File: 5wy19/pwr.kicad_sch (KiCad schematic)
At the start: 1 part, among them IC7 A2C20219

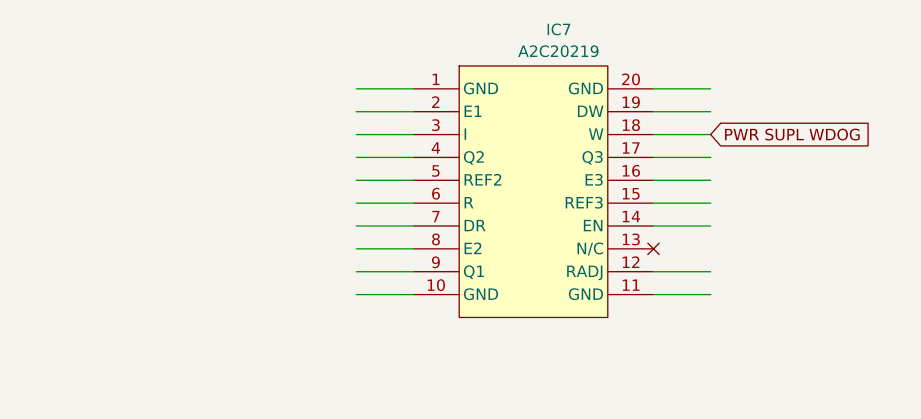
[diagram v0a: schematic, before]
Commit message: Mapped out more pins of MCU and relevant circuits
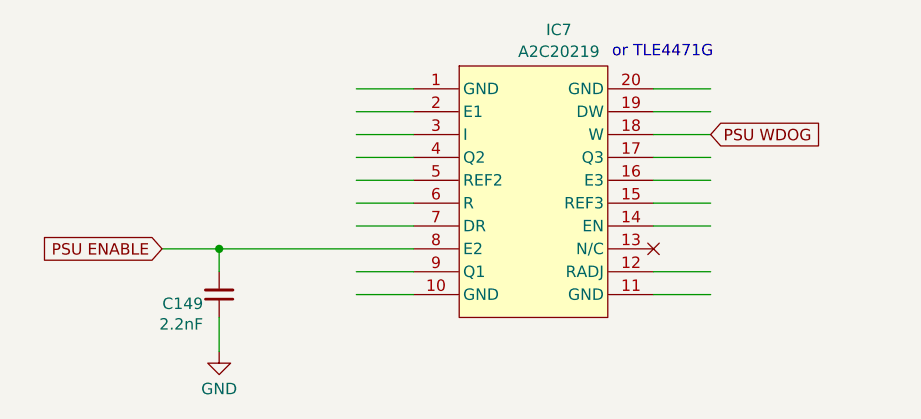
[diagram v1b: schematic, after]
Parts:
- added C149: 2.2nF, symbol Device:C_Small
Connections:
- net PSU ENABLE: now reaches IC7.8 (E2)
- net PSU ENABLE: now also C149.2
- net PWR SUPL WDOG renamed PSU WDOG
- new net GND: C149.1
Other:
- note added: "or TLE4471G"
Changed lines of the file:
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@@
 	(generator_version "9.0")
 	(paper "A4")
+	(text "or TLE4471G"
+		(exclude_from_sim no)
+		(at 155.956 77.216 0)
+		(effects
+			(font
+				(size 1.27 1.27)
+			)
+		)
+	)
+	(junction
+		(at 106.68 99.06)
+		(diameter 0)
+		(color 0 0 0 0)
+	)
 	(wire
 		(pts
@@
 	(wire
 		(pts
+			(xy 106.68 106.68) (xy 106.68 110.49)
+		)
+		(stroke
+			(width 0)
+			(type default)
+		)
+	)
+	(wire
+		(pts
 			(xy 121.92 81.28) (xy 128.27 81.28)
 		)
@@
 	(wire
 		(pts
-			(xy 121.92 99.06) (xy 128.27 99.06)
+			(xy 100.33 99.06) (xy 106.68 99.06)
+		)
+		(stroke
+			(width 0)
+			(type default)
+		)
+	)
+	(wire
+		(pts
+			(xy 106.68 99.06) (xy 128.27 99.06)
+		)
+		(stroke
+			(width 0)
+			(type default)
+		)
+	)
+	(wire
+		(pts
+			(xy 106.68 99.06) (xy 106.68 101.6)
 		)
 		(stroke
@@
 		)
 	)
-	(global_label "PWR SUPL WDOG"
+	(global_label "PSU ENABLE"
+		(shape input)
+		(at 100.33 99.06 180)
+		(fields_autoplaced yes)
+		(effects
+			(font
+				(size 1.27 1.27)
+			)
+			(justify right)
+		)
+		(property "Intersheetrefs" "${INTERSHEET_REFS}"
+			(at 85.552 99.06 0)
+			(effects
+				(font
+					(size 1.27 1.27)
+				)
+				(justify right)
+				(hide yes)
+			)
+		)
+	)
+	(global_label "PSU WDOG"
 		(shape input)
 		(at 161.29 86.36 0)
@@
 				(justify left)
 				(hide yes)
+			)
+		)
+	)
+	(symbol
+		(lib_id "power:GND")
+		(at 106.68 110.49 0)
+		(unit 1)
+		(exclude_from_sim no)
+		(in_bom yes)
+		(on_board yes)
+		(dnp no)
+		(fields_autoplaced yes)
+		(property "Reference" "#PWR044"
+			(at 106.68 116.84 0)
+			(effects
+				(font
+					(size 1.27 1.27)
+				)
+				(hide yes)
+			)
+		)
+		(property "Value" "GND"
+			(at 106.68 114.6231 0)
+			(effects
+				(font
+					(size 1.27 1.27)
+				)
+			)
+		)
+		(property "Footprint" ""
+			(at 106.68 110.49 0)
+			(effects
+				(font
+					(size 1.27 1.27)
+				)
+				(hide yes)
+			)
+		)
+		(property "Datasheet" ""
+			(at 106.68 110.49 0)
+			(effects
+				(font
+					(size 1.27 1.27)
+				)
+				(hide yes)
+			)
+		)
+		(property "Description" "Power symbol creates a global label with name \"GND\" , ground"
+			(at 106.68 110.49 0)
+			(effects
+				(font
+					(size 1.27 1.27)
+				)
+				(hide yes)
+			)
+		)
+		(pin "1"
+		)
+		(instances
+			(project "5wy19_converted"
+				(path "/abd366a8-4ac6-4ee7-9079-ac453affd4f2/c4e8148c-e0d9-424a-a1b0-b7edb94ab807"
+					(reference "#PWR044")
+					(unit 1)
+				)
 			)
 		)
@@
 					(unit 1)
 				)
+			)
+		)
+	)
+	(symbol
+		(lib_id "Device:C_Small")
+		(at 106.68 104.14 180)
+		(unit 1)
+		(exclude_from_sim no)
+		(in_bom yes)
+		(on_board yes)
+		(dnp no)
+		(property "Reference" "C149"
+			(at 104.902 105.156 0)
+			(effects
+				(font
+					(size 1.27 1.27)
+				)
+				(justify left)
+			)
+		)
+		(property "Value" "2.2nF"
+			(at 104.902 107.442 0)
+			(effects
+				(font
+					(size 1.27 1.27)
+				)
+				(justify left)
+			)
+		)
+		(property "Footprint" ""
+			(at 106.68 104.14 0)
+			(effects
+				(font
+					(size 1.27 1.27)
+				)
+				(hide yes)
+			)
+		)
+		(property "Datasheet" "~"
+			(at 106.68 104.14 0)
+			(effects
+				(font
+					(size 1.27 1.27)
+				)
+				(hide yes)
+			)
+		)
+		(property "Description" "Unpolarized capacitor, small symbol"
+			(at 106.68 104.14 0)
+			(effects
+				(font
+					(size 1.27 1.27)
+				)
+				(hide yes)
+			)
+		)
+		(pin "1"
+		)
+		(pin "2"
+		)
+		(instances
+			(project "5wy19_converted"
+				(path "/abd366a8-4ac6-4ee7-9079-ac453affd4f2/c4e8148c-e0d9-424a-a1b0-b7edb94ab807"
+					(reference "C149")
+					(unit 1)
+				)

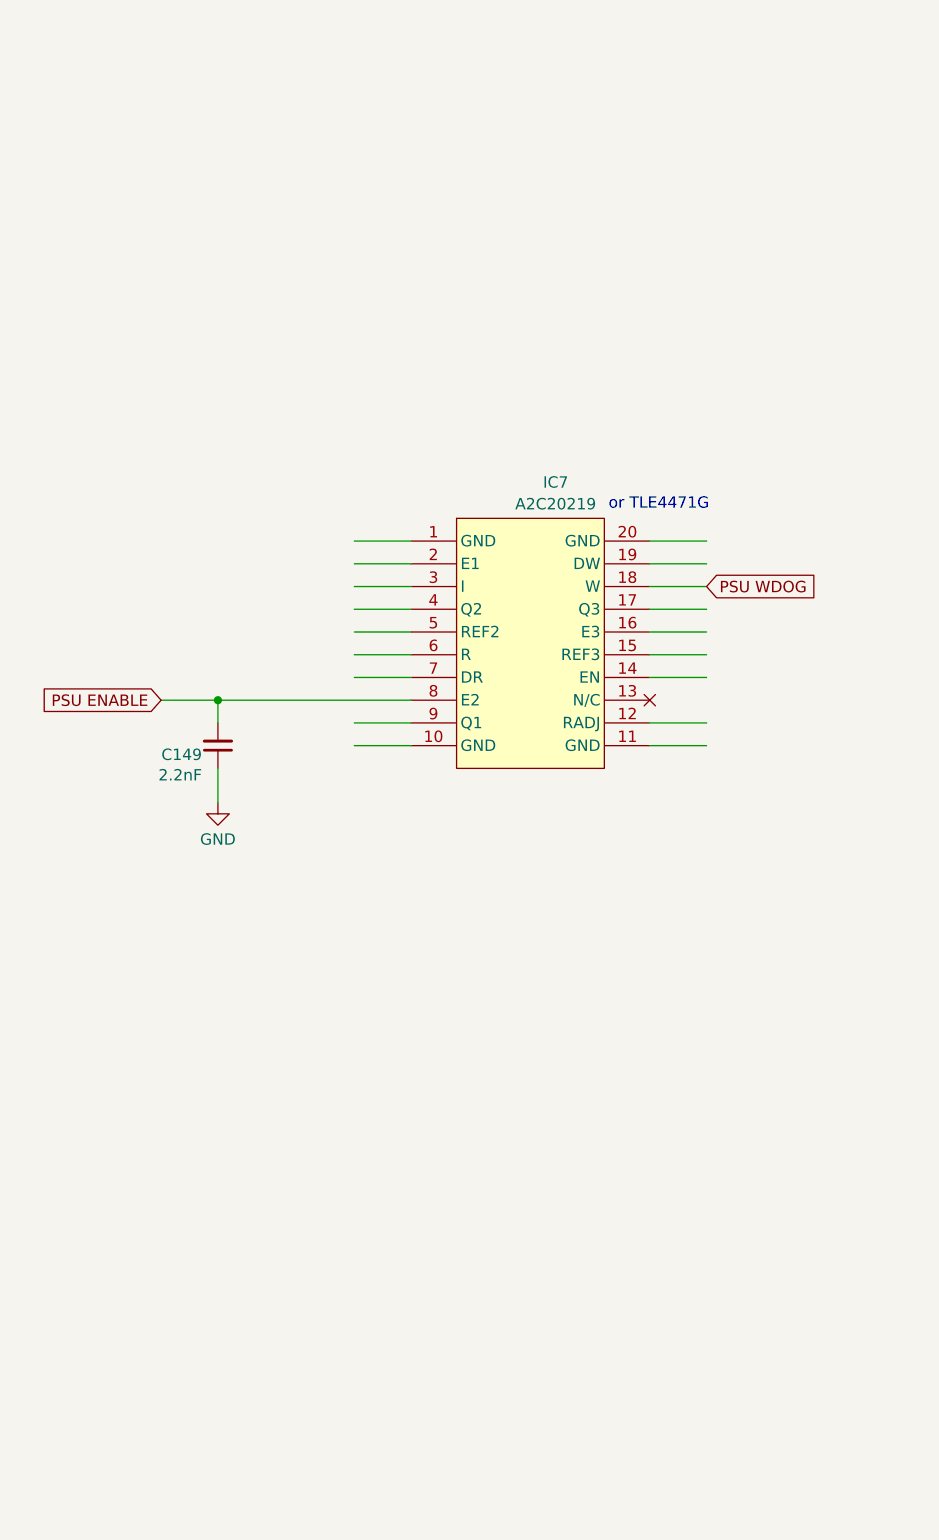
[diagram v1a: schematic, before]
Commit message: Finished most of the subsystems
-- MCU finished
-- Flash finished
-- Power Supply finished
-- I/O Drivers finished
-- CANBUS finished
-- Knock Control finished
-- Connector finished
-- Ignition Driver finished
-- Sensor Logic mostly finished
-- Logic ICs need some work
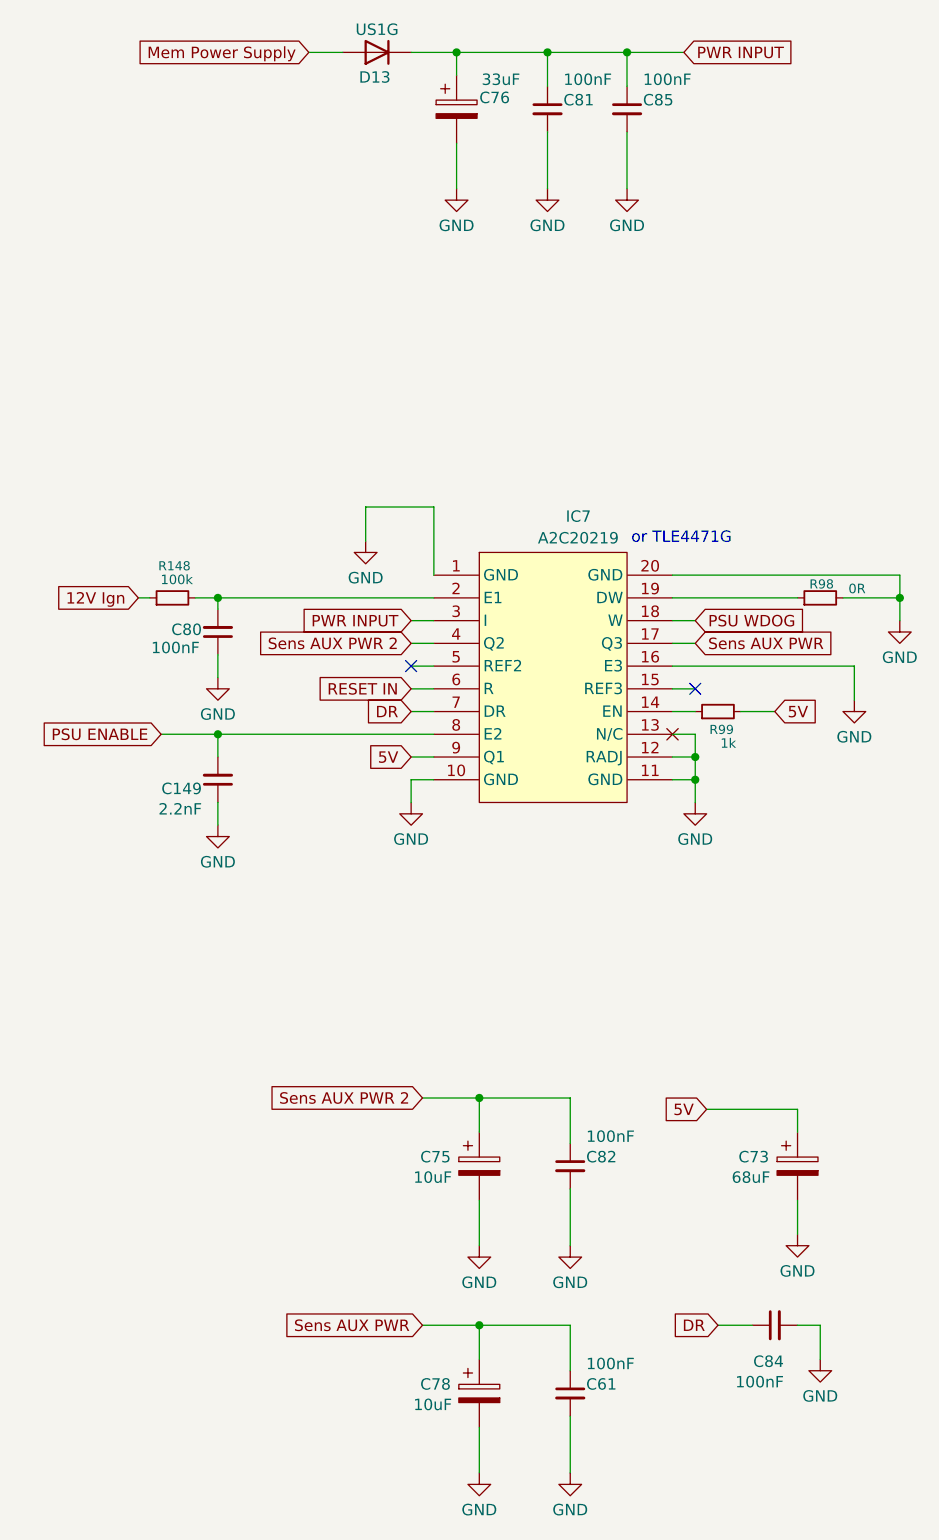
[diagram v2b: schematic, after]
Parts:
- added C61, C80, C81, C82, C84, C85: 100nF, symbol Device:C_Small
- added C73: 68uF, symbol Device:C_Polarized
- added C75, C78: 10uF, symbol Device:C_Polarized
- added C76: 33uF, symbol Device:C_Polarized
- added D13: US1G, Diode_SMD:D_SMA, symbol Diode:US1G
- added R148: 100k, symbol Device:R_Small
- added R98: 0R, symbol Device:R_Small
- added R99: 1k, symbol Device:R_Small
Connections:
- net GND: now also IC7.1 (GND), IC7.10 (GND), IC7.11 (GND), IC7.12 (RADJ), IC7.13 (N/C), IC7.16 (E3), IC7.20 (GND), C61.2, C73.2, C75.2, C76.2, C78.2, C80.1, C81.2, C82.2, C84.2, C85.2, R98.2
- net at IC7.14 (EN): now also R99.1
- net Sens AUX PWR: now reaches IC7.17 (Q3)
- net Sens AUX PWR: now also C61.1, C78.1
- net at IC7.19 (DW): now also R98.1
- net at IC7.2 (E1): now also C80.2, R148.2
- net PWR INPUT: now reaches IC7.3 (I)
- net PWR INPUT: now also C76.1, C81.1, C85.1, D13.1 (K)
- net Sens AUX PWR 2: now reaches IC7.4 (Q2)
- net Sens AUX PWR 2: now also C75.1, C82.1
- net RESET IN: now reaches IC7.6 (R)
- net DR: now reaches IC7.7 (DR)
- net DR: now also C84.1
- net 5V: now reaches IC7.9 (Q1)
- net 5V: now also C73.1, R99.2
- new net 12V Ign: R148.1
- new net Mem Power Supply: D13.2 (A)
- no-connect marks 0 -> 2
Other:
- title: (none) -> SMIK43 5WY19 Rev. Eng
- moved on the sheet: C149, IC7

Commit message: Final schematic (except maybe some oversights)
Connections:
- net 12V Ign: now also R148.2; no longer R148.1
- net 5V: now also R99.1; no longer R99.2
- net GND: now also C80.2, R98.1; no longer C80.1, R98.2
- net at IC7.14 (EN): now also R99.2; no longer R99.1
- net at IC7.19 (DW): now also R98.2; no longer R98.1
- new net: C80.1, IC7.2 (E1), R148.1
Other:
- moved on the sheet: C80, R148, R98, R99
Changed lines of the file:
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@@
 	(symbol
 		(lib_id "Device:R_Small")
-		(at 101.6 87.63 90)
+		(at 101.6 87.63 270)
 		(unit 1)
 		(exclude_from_sim no)
@@
 		(dnp no)
 		(property "Reference" "R148"
-			(at 103.632 84.074 90)
+			(at 99.568 91.186 90)
 			(effects
 				(font
@@
 		)
 		(property "Value" "100k"
-			(at 103.886 85.598 90)
+			(at 99.314 89.662 90)
 			(effects
 				(font
@@
 	(symbol
 		(lib_id "Device:R_Small")
-		(at 162.56 100.33 90)
+		(at 162.56 100.33 270)
 		(unit 1)
 		(exclude_from_sim no)
@@
 		(dnp no)
 		(property "Reference" "R99"
-			(at 164.338 102.362 90)
+			(at 162.814 98.298 90)
 			(effects
 				(font
@@
 		)
 		(property "Value" "1k"
-			(at 164.592 103.886 90)
+			(at 162.56 96.774 90)
 			(effects
 				(font
@@
 	(symbol
 		(lib_id "Device:C_Small")
-		(at 106.68 91.44 180)
+		(at 106.68 91.44 0)
 		(unit 1)
 		(exclude_from_sim no)
@@
 		(dnp no)
 		(property "Reference" "C80"
-			(at 104.902 91.186 0)
+			(at 108.458 91.694 0)
 			(effects
 				(font
@@
 		)
 		(property "Value" "100nF"
-			(at 104.648 93.218 0)
+			(at 108.712 89.662 0)
 			(effects
 				(font
@@
 	(symbol
 		(lib_id "Device:R_Small")
-		(at 173.99 87.63 90)
+		(at 173.99 87.63 270)
 		(unit 1)
 		(exclude_from_sim no)
@@
 		(dnp no)
 		(property "Reference" "R98"
-			(at 175.514 86.106 90)
+			(at 172.466 86.106 90)
 			(effects
 				(font
@@
 		)
 		(property "Value" "0R"
-			(at 179.07 86.614 90)
-			(effects
-				(font
+			(at 176.784 86.614 90)
+			(effects
+				(font
